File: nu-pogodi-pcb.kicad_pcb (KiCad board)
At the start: 10 copper layers, 120 x 80 mm, 24 parts, among them J1 Pico_Socket_A, J2 Pico_Socket_B, J3 MSP2806 Socket A, J4 MSP2806 Socket B, J5 Conn_01x02_Pin, Q1 2N2222, SW1 SPST-NO 6x6mm, SW10 SW_DPDT_x2, SW2 SPST-NO 6x6mm, SW3 SPST-NO 6x6mm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

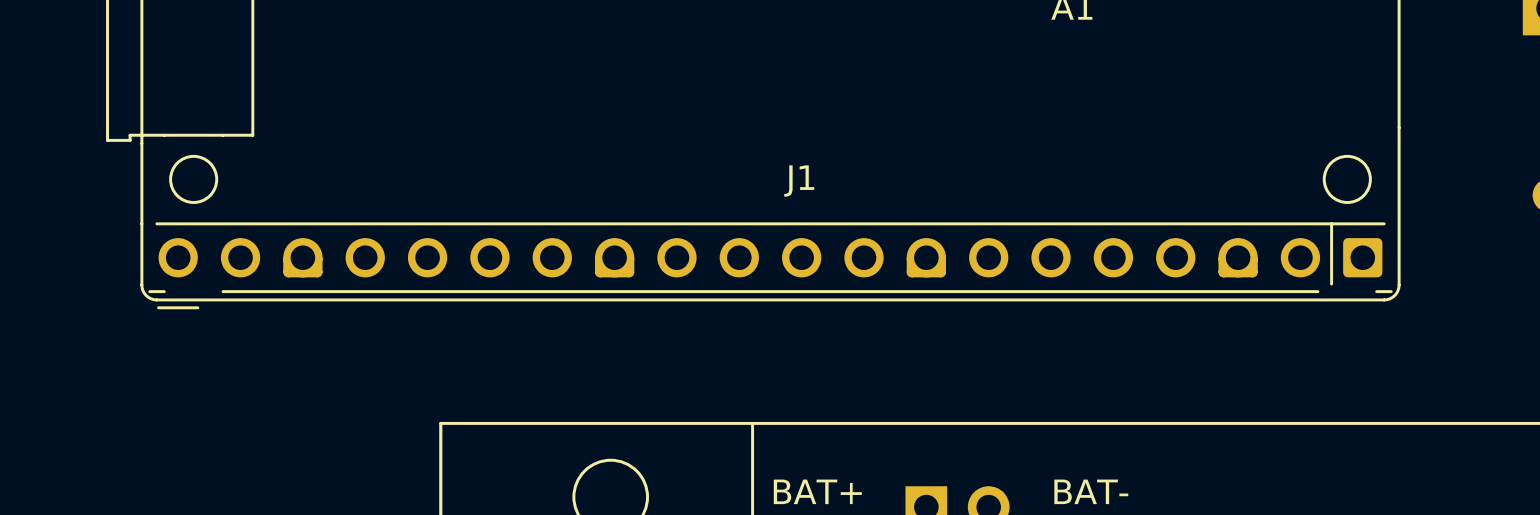
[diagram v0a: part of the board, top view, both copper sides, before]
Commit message: Fixed pinout
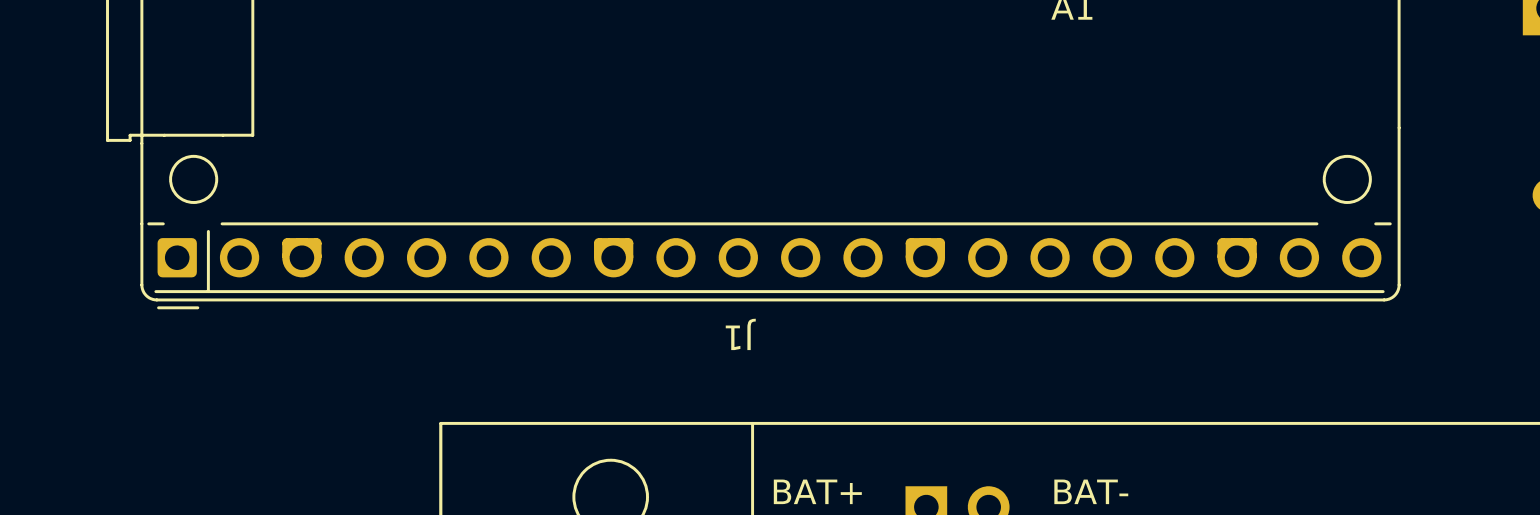
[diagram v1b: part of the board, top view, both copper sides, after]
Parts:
- moved J1 48.3 mm to (44.6, 54.9), turned to 90 degrees
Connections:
- J1 pad 10: /ROW_2 -> /ROW_1
- J1 pad 9: /ROW_1 -> /ROW_2
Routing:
- net /COL_1: track 206.7 -> 137.0 mm
- net /COL_4: track 162.1 -> 99.7 mm
- net /BUZZER: track 64.4 -> 20.9 mm
- net /COL_3: track 141.1 -> 112.8 mm
- net /COL_2: track 155.7 -> 140.3 mm
- net /ROW_2: track 105.1 -> 108.7 mm
- net /ROW_1: track 238.6 -> 241.8 mm
